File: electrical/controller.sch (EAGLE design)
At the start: 36 parts, among them IC1 MCP6232, IC2 LTC1661MSOP8, IC3 MCP6232, IC4 ICM7555, IC5 CD40109B, J3 455-1750-1-ND, Q1 DMP3098, Q3 600mA/40V, U1 U3V16F15, U2 U3V16F15

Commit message: Change arduino footprint
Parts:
- UC1: device BEST_Custom:ARDUINO_PRO_MICRO2D -> BEST_Custom:ARDUINO_PRO_MICROUSBC
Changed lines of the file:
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@@
 <attribute name="REVISION" value="D2"/>
 </part>
-<part name="UC1" library="BEST_Custom" library_urn="urn:adsk.eagle:library:10805467" deviceset="ARDUINO_PRO_MICRO" device="2D" package3d_urn="urn:adsk.eagle:package:49177699/2"/>
+<part name="UC1" library="BEST_Custom" library_urn="urn:adsk.eagle:library:10805467" deviceset="ARDUINO_PRO_MICRO" device="USBC" package3d_urn="urn:adsk.eagle:package:49279253/1"/>
 <part name="ST1" library="BEST_Custom" library_urn="urn:adsk.eagle:library:10805467" deviceset="2PIN_SCREW" device="" package3d_urn="urn:adsk.eagle:package:49052268/3"/>
 <part name="ST2" library="BEST_Custom" library_urn="urn:adsk.eagle:library:10805467" deviceset="2PIN_SCREW" device="" package3d_urn="urn:adsk.eagle:package:49052268/3"/>

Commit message: Plop some things onto the PCB, lots of work to do.
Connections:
- removed net 12V: IC5.VDD, JP1.1
- net 15V: now also IC5.VDD, JP1.1
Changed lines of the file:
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@@
 <pinref part="SUPPLY31" gate="G$1" pin="12V"/>
+</segment>
+<segment>
+<pinref part="JP1" gate="G$1" pin="1"/>
+<pinref part="SUPPLY20" gate="G$1" pin="12V"/>
+<wire x1="76.2" y1="154.94" x2="81.28" y2="154.94" width="0.1524" layer="91"/>
+</segment>
+<segment>
+<pinref part="IC5" gate="G$1" pin="VDD"/>
+<pinref part="SUPPLY16" gate="G$1" pin="12V"/>
+<wire x1="215.9" y1="172.72" x2="213.36" y2="172.72" width="0.1524" layer="91"/>
 </segment>
 </net>
@@
 </segment>
 </net>
-<net name="12V" class="0">
-<segment>
-<pinref part="JP1" gate="G$1" pin="1"/>
-<pinref part="SUPPLY20" gate="G$1" pin="12V"/>
-<wire x1="76.2" y1="154.94" x2="81.28" y2="154.94" width="0.1524" layer="91"/>
-</segment>
-<segment>
-<pinref part="IC5" gate="G$1" pin="VDD"/>
-<pinref part="SUPPLY16" gate="G$1" pin="12V"/>
-<wire x1="215.9" y1="172.72" x2="213.36" y2="172.72" width="0.1524" layer="91"/>
-</segment>
-</net>

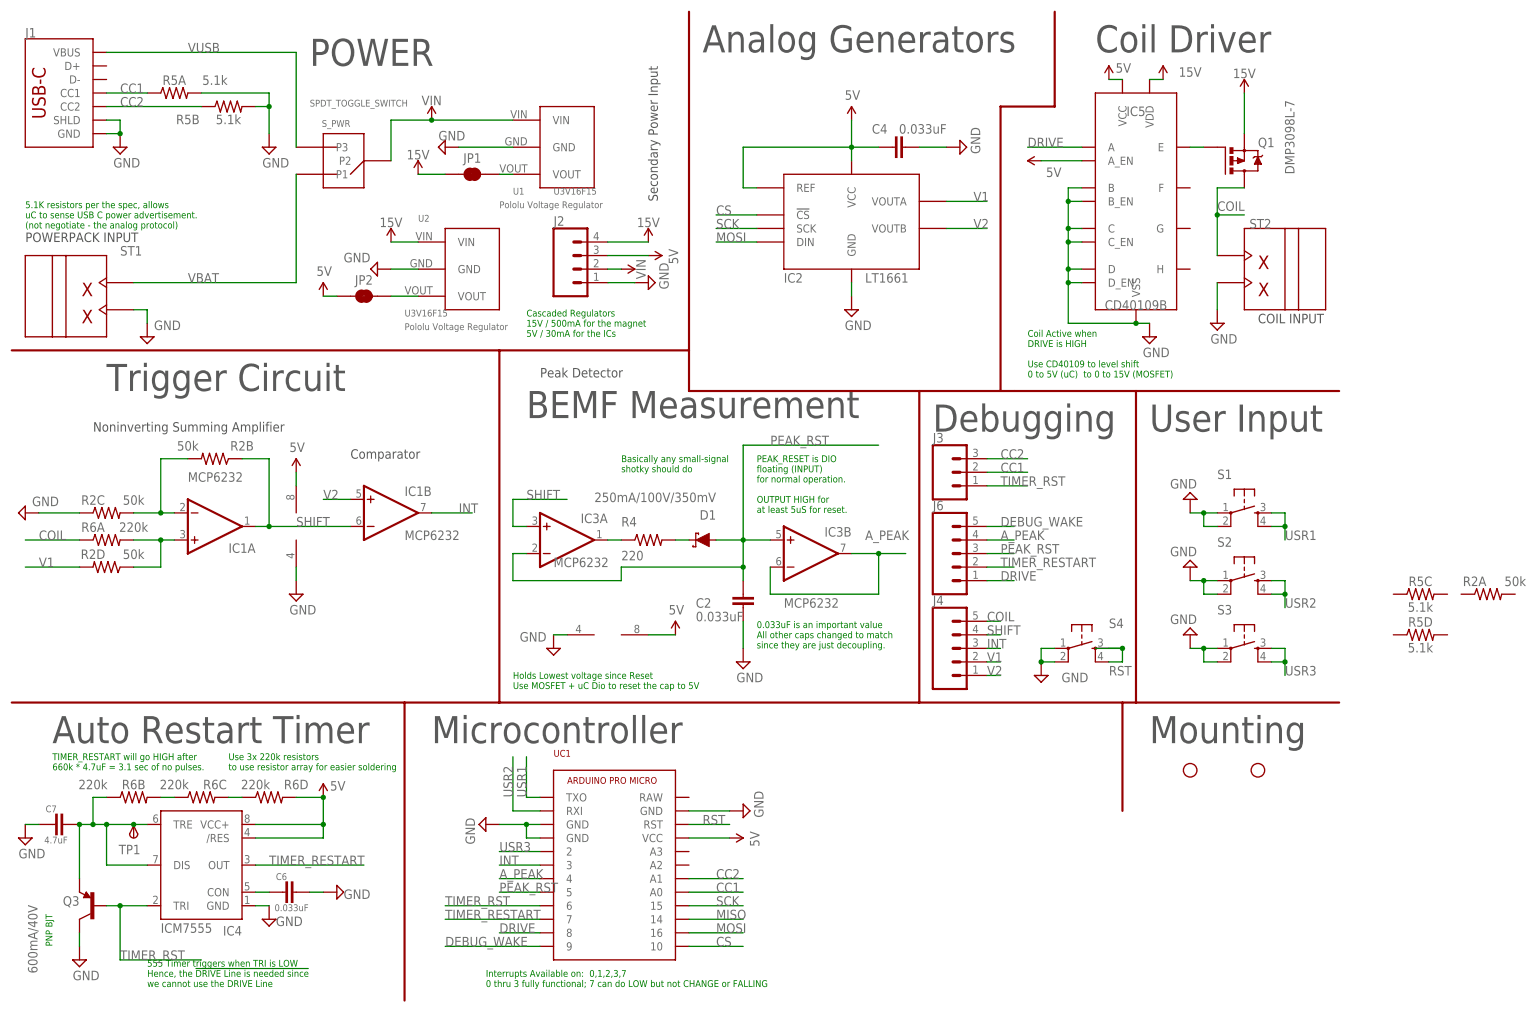
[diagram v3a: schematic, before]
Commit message: First attempt at routing D3
Now lets put it in Solidworks and check button accessibility.
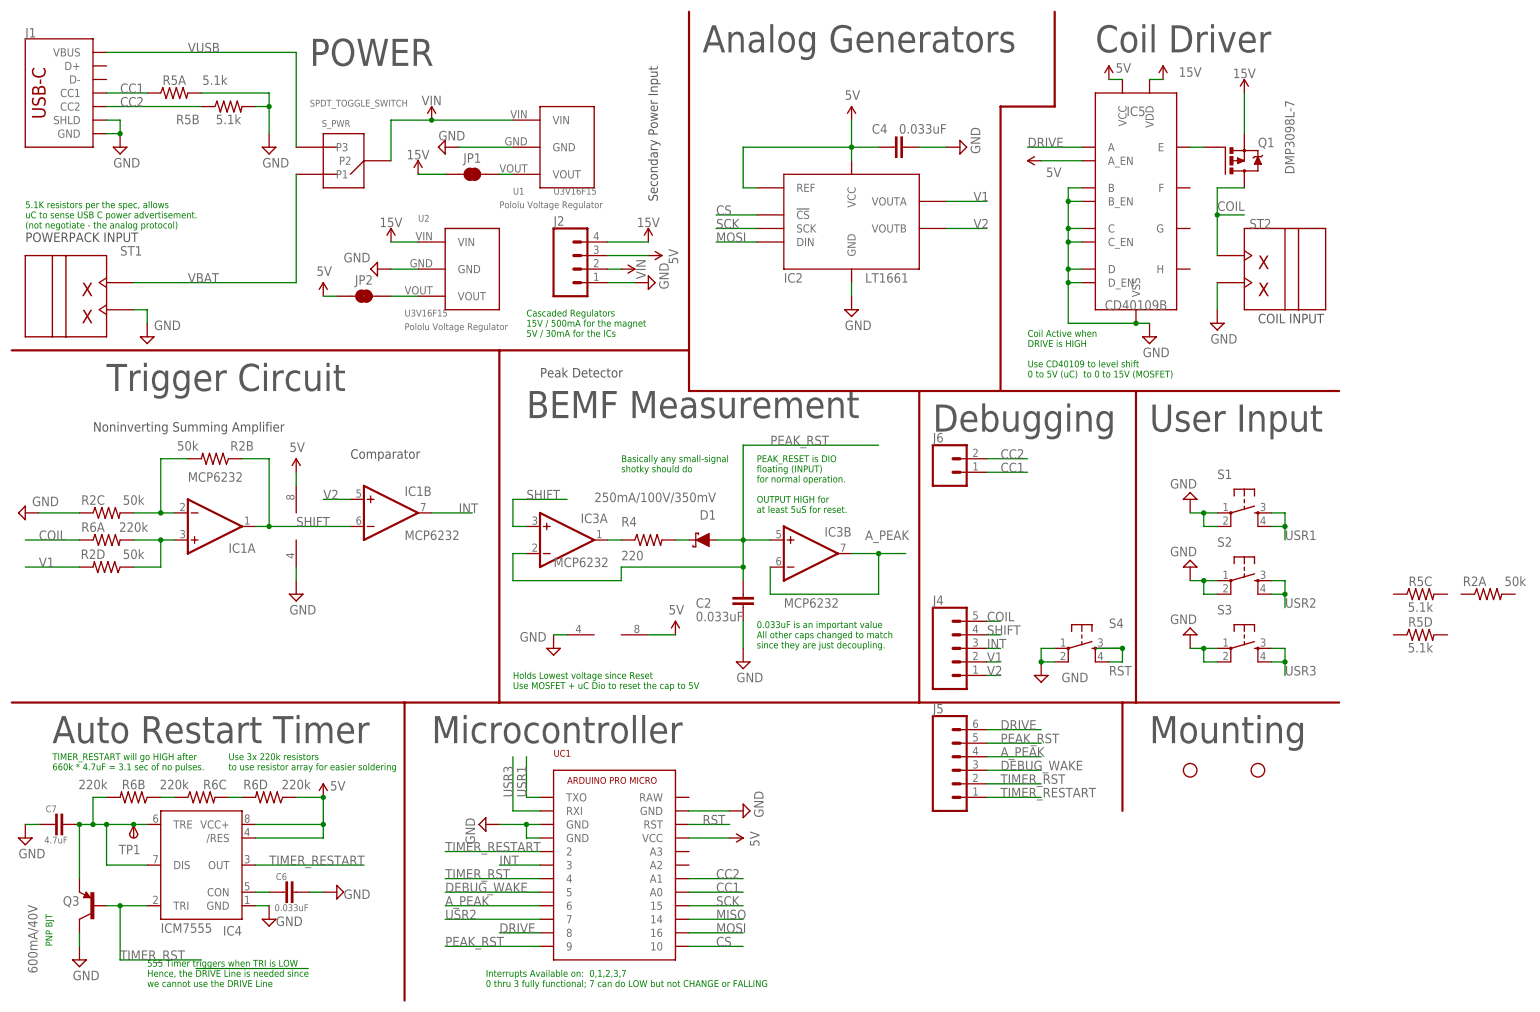
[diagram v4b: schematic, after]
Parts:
- removed J3: 455-1750-1-ND, SparkFun-Connectors:CONN_03
- added J5: (no value), SparkFun-Connectors:CONN_06NO_SILK_NO_POP
- J6: device SparkFun-Connectors:CONN_05PTH -> SparkFun-Connectors:CONN_02
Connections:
- net 5V: now also R6D.1; no longer R6D.2
- net A_PEAK: now also J5.4, UC1.6; no longer J6.4, UC1.4
- net CC1: now also J6.1; no longer J3.2
- net CC2: now also J6.2; no longer J3.3
- net DEBUG_WAKE: now also J5.3, UC1.5; no longer J6.5, UC1.9
- net DRIVE: now also J5.6; no longer J6.1
- net N$10: now also R6D.2; no longer R6D.1
- net N$3: now also R6B.1; no longer R6B.2
- net N$7: now also R6B.2; no longer R6B.1
- net PEAK_RST: now also J5.5, UC1.9; no longer J6.3, UC1.5
- net TIMER_RESTART: now also J5.1, UC1.2; no longer J6.2, UC1.7
- net TIMER_RST: now also J5.2, UC1.4; no longer J3.1, UC1.6
- net USR2: now also UC1.7; no longer UC1.RXI
- net USR3: now also UC1.RXI; no longer UC1.2
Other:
- moved on the sheet: R6B, R6D

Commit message: Clean up SCH
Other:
- note added: "Unused"
- moved on the sheet: J5, R2A, R5C, R5D
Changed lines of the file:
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@@
 <parts>
 <part name="FRAME1" library="pie" deviceset="FRAME_SCHEMATIC" device="">
-<attribute name="REVISION" value="D2"/>
+<attribute name="REVISION" value="D3"/>
 </part>
 <part name="UC1" library="BEST_Custom" library_urn="urn:adsk.eagle:library:10805467" deviceset="ARDUINO_PRO_MICRO" device="USBC" package3d_urn="urn:adsk.eagle:package:49279263/1"/>
@@
 <wire x1="210.82" y1="114.3" x2="210.82" y2="55.88" width="0.4064" layer="94"/>
 <wire x1="210.82" y1="55.88" x2="248.92" y2="55.88" width="0.4064" layer="94"/>
-<wire x1="91.44" y1="55.88" x2="170.18" y2="55.88" width="0.4064" layer="94"/>
+<wire x1="91.44" y1="55.88" x2="147.32" y2="55.88" width="0.4064" layer="94"/>
 <text x="213.36" y="48.26" size="5.08" layer="97">Mounting</text>
 <text x="88.9" y="2.54" size="1.27" layer="91">Interrupts Available on:  0,1,2,3,7
 0 thru 3 fully functional; 7 can do LOW but not CHANGE or FALLING</text>
-<text x="2.54" y="144.78" size="1.27" layer="91">5.1K resistors per the spec, allows
+<text x="2.54" y="147.32" size="1.27" layer="91">5.1K resistors per the spec, allows
 uC to sense USB C power advertisement.
 (not negotiate - the analog protocol)</text>
@@
 we cannot use the DRIVE Line</text>
 <text x="7.62" y="48.26" size="5.08" layer="97">Auto Restart Timer</text>
+<wire x1="147.32" y1="55.88" x2="170.18" y2="55.88" width="0.4064" layer="94"/>
 <wire x1="170.18" y1="55.88" x2="210.82" y2="55.88" width="0.4064" layer="94"/>
 <wire x1="73.66" y1="55.88" x2="73.66" y2="0" width="0.4064" layer="94"/>
@@
 <wire x1="185.42" y1="167.64" x2="185.42" y2="114.3" width="0.4064" layer="94"/>
 <wire x1="185.42" y1="114.3" x2="187.96" y2="114.3" width="0.1524" layer="94"/>
+<wire x1="147.32" y1="55.88" x2="147.32" y2="35.56" width="0.4064" layer="94"/>
+<text x="160.02" y="48.26" size="5.08" layer="97">Unused</text>
 </plain>
 <instances>
@@
 <attribute name="VALUE" x="119.38" y="145.034" size="1.778" layer="96" font="vector" align="bottom-center"/>
 </instance>
-<instance part="R2" gate="A" x="276.86" y="76.2" smashed="yes">
-<attribute name="NAME" x="274.32" y="77.724" size="1.778" layer="95" font="vector" align="bottom-center"/>
-<attribute name="VALUE" x="281.94" y="77.724" size="1.778" layer="96" font="vector" rot="R180" align="top-center"/>
+<instance part="R2" gate="A" x="193.04" y="43.18" smashed="yes">
+<attribute name="NAME" x="190.5" y="44.704" size="1.778" layer="95" font="vector" align="bottom-center"/>
+<attribute name="VALUE" x="198.12" y="44.704" size="1.778" layer="96" font="vector" rot="R180" align="top-center"/>
 </instance>
 <instance part="R2" gate="B" x="38.1" y="101.6" smashed="yes" rot="R180">
@@
 <attribute name="VALUE" x="40.64" y="166.116" size="1.778" layer="96" font="vector" align="top-center"/>
 </instance>
-<instance part="R5" gate="C" x="264.16" y="76.2" smashed="yes">
-<attribute name="NAME" x="264.16" y="77.724" size="1.778" layer="95" font="vector" align="bottom-center"/>
-<attribute name="VALUE" x="264.16" y="74.676" size="1.778" layer="96" font="vector" align="top-center"/>
-</instance>
-<instance part="R5" gate="D" x="264.16" y="68.58" smashed="yes">
-<attribute name="NAME" x="264.16" y="70.104" size="1.778" layer="95" font="vector" align="bottom-center"/>
-<attribute name="VALUE" x="264.16" y="67.056" size="1.778" layer="96" font="vector" align="top-center"/>
+<instance part="R5" gate="C" x="177.8" y="43.18" smashed="yes">
+<attribute name="NAME" x="177.8" y="44.704" size="1.778" layer="95" font="vector" align="bottom-center"/>
+<attribute name="VALUE" x="177.8" y="41.656" size="1.778" layer="96" font="vector" align="top-center"/>
+</instance>
+<instance part="R5" gate="D" x="162.56" y="43.18" smashed="yes">
+<attribute name="NAME" x="162.56" y="44.704" size="1.778" layer="95" font="vector" align="bottom-center"/>
+<attribute name="VALUE" x="162.56" y="41.656" size="1.778" layer="96" font="vector" align="top-center"/>
 </instance>
 <instance part="R6" gate="A" x="17.78" y="86.36" smashed="yes">
@@
 <attribute name="TP_SIGNAL_NAME" x="21.59" y="31.75" size="1.778" layer="97" rot="R180"/>
 </instance>
-<instance part="J5" gate="J1" x="177.8" y="43.18" smashed="yes">
-<attribute name="VALUE" x="172.72" y="33.274" size="1.778" layer="96" font="vector"/>
-<attribute name="NAME" x="172.72" y="53.848" size="1.778" layer="95" font="vector"/>
+<instance part="J5" gate="J1" x="180.34" y="83.82" smashed="yes">
+<attribute name="VALUE" x="175.26" y="73.914" size="1.778" layer="96" font="vector"/>
+<attribute name="NAME" x="175.26" y="94.488" size="1.778" layer="95" font="vector"/>
 </instance>
 <instance part="J6" gate="J1" x="175.26" y="99.06" smashed="yes">
@@
 <segment>
 <pinref part="J5" gate="J1" pin="6"/>
-<wire x1="182.88" y1="50.8" x2="193.04" y2="50.8" width="0.1524" layer="91"/>
-<label x="185.42" y="50.8" size="1.778" layer="95"/>
+<wire x1="185.42" y1="91.44" x2="195.58" y2="91.44" width="0.1524" layer="91"/>
+<label x="187.96" y="91.44" size="1.778" layer="95"/>
 </segment>
 </net>
@@
 <segment>
 <pinref part="J5" gate="J1" pin="5"/>
-<wire x1="182.88" y1="48.26" x2="193.04" y2="48.26" width="0.1524" layer="91"/>
-<label x="185.42" y="48.26" size="1.778" layer="95"/>
+<wire x1="185.42" y1="88.9" x2="195.58" y2="88.9" width="0.1524" layer="91"/>
+<label x="187.96" y="88.9" size="1.778" layer="95"/>
 </segment>
 <segment>
@@
 <segment>
 <pinref part="J5" gate="J1" pin="4"/>
-<wire x1="182.88" y1="45.72" x2="193.04" y2="45.72" width="0.1524" layer="91"/>
-<label x="185.42" y="45.72" size="1.778" layer="95"/>
+<wire x1="185.42" y1="86.36" x2="195.58" y2="86.36" width="0.1524" layer="91"/>
+<label x="187.96" y="86.36" size="1.778" layer="95"/>
 </segment>
 <segment>
@@
 <segment>
 <pinref part="J5" gate="J1" pin="2"/>
-<wire x1="182.88" y1="40.64" x2="193.04" y2="40.64" width="0.1524" layer="91"/>
-<label x="185.42" y="40.64" size="1.778" layer="95"/>
+<wire x1="185.42" y1="81.28" x2="195.58" y2="81.28" width="0.1524" layer="91"/>
+<label x="187.96" y="81.28" size="1.778" layer="95"/>
 </segment>
 </net>
@@
 <segment>
 <pinref part="J5" gate="J1" pin="1"/>
-<wire x1="182.88" y1="38.1" x2="193.04" y2="38.1" width="0.1524" layer="91"/>
-<label x="185.42" y="38.1" size="1.778" layer="95"/>
+<wire x1="185.42" y1="78.74" x2="195.58" y2="78.74" width="0.1524" layer="91"/>
+<label x="187.96" y="78.74" size="1.778" layer="95"/>
 </segment>
 </net>
@@
 <segment>
 <pinref part="J5" gate="J1" pin="3"/>
-<wire x1="182.88" y1="43.18" x2="193.04" y2="43.18" width="0.1524" layer="91"/>
-<label x="185.42" y="43.18" size="1.778" layer="95"/>
-</segment>
-<segment>
+<wire x1="185.42" y1="83.82" x2="195.58" y2="83.82" width="0.1524" layer="91"/>
+<label x="187.96" y="83.82" size="1.778" layer="95"/>
+</segment>
+<segment>

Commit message: Update routing, silkscreen, in minor ways.
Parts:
- J2: device SparkFun-Connectors:CONN_04PTH -> SparkFun-Connectors:CONN_041X04_NO_SILK
- J4: device SparkFun-Connectors:CONN_05PTH -> SparkFun-Connectors:CONN_05NO_SILK
- J6: device SparkFun-Connectors:CONN_02 -> SparkFun-Connectors:CONN_021X02_NO_SILK
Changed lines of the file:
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@@
 <part name="U$5" library="BEST_Custom" library_urn="urn:adsk.eagle:library:10805467" deviceset="5V" device=""/>
 <part name="SUPPLY26" library="SparkFun-PowerSymbols" deviceset="15V" device=""/>
-<part name="J4" library="SparkFun-Connectors" library_urn="urn:adsk.eagle:library:49052309" deviceset="CONN_05" device="PTH" package3d_urn="urn:adsk.eagle:package:49052939/1"/>
-<part name="J2" library="SparkFun-Connectors" library_urn="urn:adsk.eagle:library:49052309" deviceset="CONN_04" device="PTH" package3d_urn="urn:adsk.eagle:package:49052925/1"/>
+<part name="J4" library="SparkFun-Connectors" library_urn="urn:adsk.eagle:library:49052309" deviceset="CONN_05" device="NO_SILK" package3d_urn="urn:adsk.eagle:package:49052940/1"/>
+<part name="J2" library="SparkFun-Connectors" library_urn="urn:adsk.eagle:library:49052309" deviceset="CONN_04" device="1X04_NO_SILK" package3d_urn="urn:adsk.eagle:package:49052934/1"/>
 <part name="U$6" library="BEST_Custom" library_urn="urn:adsk.eagle:library:10805467" deviceset="5V" device=""/>
 <part name="SUPPLY31" library="SparkFun-PowerSymbols" deviceset="15V" device=""/>
@@
 <part name="TP1" library="testpad" library_urn="urn:adsk.eagle:library:385" deviceset="TPS" device="PAD1-13" package3d_urn="urn:adsk.eagle:package:27946/1" value="TPSPAD1-13"/>
 <part name="J5" library="SparkFun-Connectors" library_urn="urn:adsk.eagle:library:49052309" deviceset="CONN_06" device="NO_SILK_NO_POP" package3d_urn="urn:adsk.eagle:package:49053105/1"/>
-<part name="J6" library="SparkFun-Connectors" library_urn="urn:adsk.eagle:library:49052309" deviceset="CONN_02" device="" package3d_urn="urn:adsk.eagle:package:49052890/1"/>
+<part name="J6" library="SparkFun-Connectors" library_urn="urn:adsk.eagle:library:49052309" deviceset="CONN_02" device="1X02_NO_SILK" package3d_urn="urn:adsk.eagle:package:49052902/1"/>
 </parts>
 <sheets>
